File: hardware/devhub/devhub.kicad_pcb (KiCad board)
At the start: 4 copper layers, 100 x 100 mm, 170 parts, among them J1 USB-C PWR IN, J101 USB-C, J2 USB-C UPSTREAM, J201 USB-C, J301 USB-C, J4 SWD, J401 USB-C, J5 Banana COM 1, J6 Banana NC 1, J9 UART debug, K1 G5Q-1 DC5, SW1 Push button switch, generic, 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, SW101 Push button switch, generic, 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, SW201 Push button switch, generic, 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, SW301 Push button switch, generic, 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, SW401 Push button switch, generic, 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, U1 AP7361C-33ER, U101 PI3USB4002A, U12 MCP120T-300I/TT, U13 TPS259470ARPWR, U2 USB2517I-JZX, U201 PI3USB4002A, U3 STM32G0B1CEU6, U301 PI3USB4002A, U4 UCS2114-1-V/LX, U401 PI3USB4002A, U5 UCS2114-1-V/LX, U9 ULN2003V12, Y1 24MHz 12pF

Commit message: U1 thermal vias, wider input zones, GND links at USB-C pins
- U1_HEATSINK: zone reshaped to about 2.6 cm2, 11 vias 0.6/0.3 around
  the tab to the +3V3 plane on In1.Cu instead of 4 vias at the zone edges
- VBUS_IN zone on B.Cu enlarged towards U13, +5V zone corner adjusted
- Port connectors: GND pins tied to the nearby shield pads with 0.6 mm tracks
- C5/C6/C7: GND pads joined with 0.6 mm tracks
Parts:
- C81, R81: moved to F.Cu
- moved TP12 17.8 mm to (143.0, 138.5)
- moved TP14 17.8 mm to (113.0, 138.5)
- moved TP4 11.8 mm to (117.9, 90.6)
- moved TP13 9.77 mm to (128.0, 138.5)
- moved TP11 9.77 mm to (158.0, 138.5)
- moved C81 7.78 mm to (81.8, 122.0)
- moved R81 7.78 mm to (77.0, 122.0)
- moved H1 3.04 mm to (76.7, 103.3)
- moved TP9 2.26 mm to (96.8, 75.5)
- moved J9 2.00 mm to (126.3, 51.5)
- moved TP6 0.10 mm to (95.7, 85.8)
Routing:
- net GND: track 239.3 -> 252.4 mm
- net /Relè ausiliario/BAN1_COM: track 28.8 -> 24.1 mm
- net /Relè ausiliario/K1_NC: track 22.5 -> 17.8 mm
- net VBUS_P2: track 26.6 -> 29.9 mm
- net VBUS_P4: track 26.6 -> 29.9 mm
- net VBUS_P1: track 34.9 -> 32.5 mm
- net VBUS_P3: track 34.9 -> 32.5 mm
- net /MCU STM32G0B1/UART_RX: track 48.4 -> 50.4 mm
- net /MCU STM32G0B1/UART_TX: track 45.1 -> 47.1 mm
- net /Relè ausiliario/BAN1_2: track 29.7 -> 31.7 mm
- net /Relè ausiliario/K1_NO: track 17.5 -> 18.7 mm
- net I2C1_SCL: track 76.9 -> 77.9 mm
- net EFUSE_FLT_N: track 40.7 -> 40.0 mm
- net RLY1: track 105.4 -> 106.0 mm
- net /Alimentazione/VBUS_IN: vias 0 -> 6
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- added copper zone on F.Cu, net +5V
- added copper zone on F.Cu, net /Alimentazione/VBUS_IN
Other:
- board text added: "${TITLE} REV ${REVISION} ${ISSUE_DATE}"

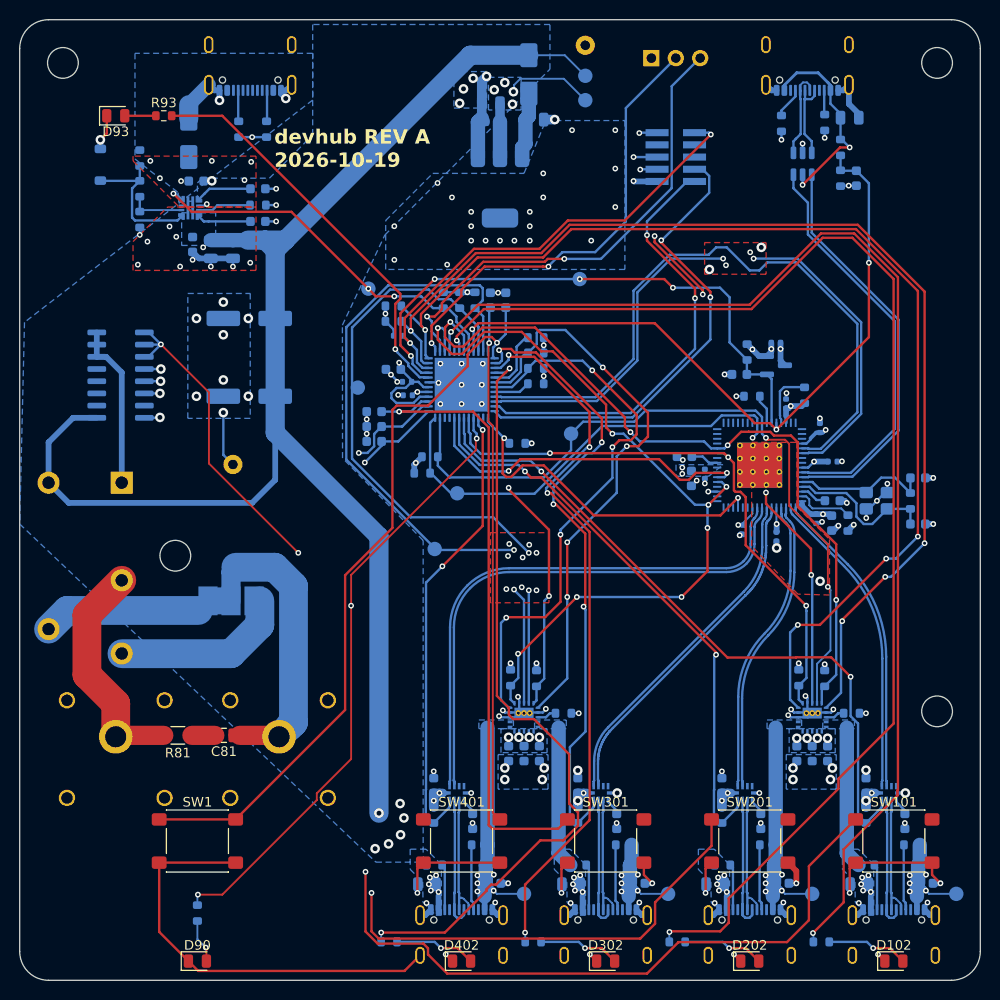
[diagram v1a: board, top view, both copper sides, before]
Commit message: PCB release check: USB_MCU jump on In1.Cu, parity fixes, docs aligned (D94, D95)
PCB: move the USB_MCU_DP crossover jump from In2.Cu to In1.Cu so the GND
plane stays continuous, tune USB_MCU_DN length to pass the skew rule,
remove the leftover "Check LDO pad connection" silkscreen note and update
footprint fields/attributes from the schematic (parity now clean).

Docs: D94 (slow signals and Full-Speed jump on In1.Cu), D95 (H1 hole
position), D52 and D84 marked as superseded on those points; layer table,
port 6 paragraph and manual checks in regole-pcb.md; PCB status, D93 LED
and H1 position in README.md and hardware/README.md.
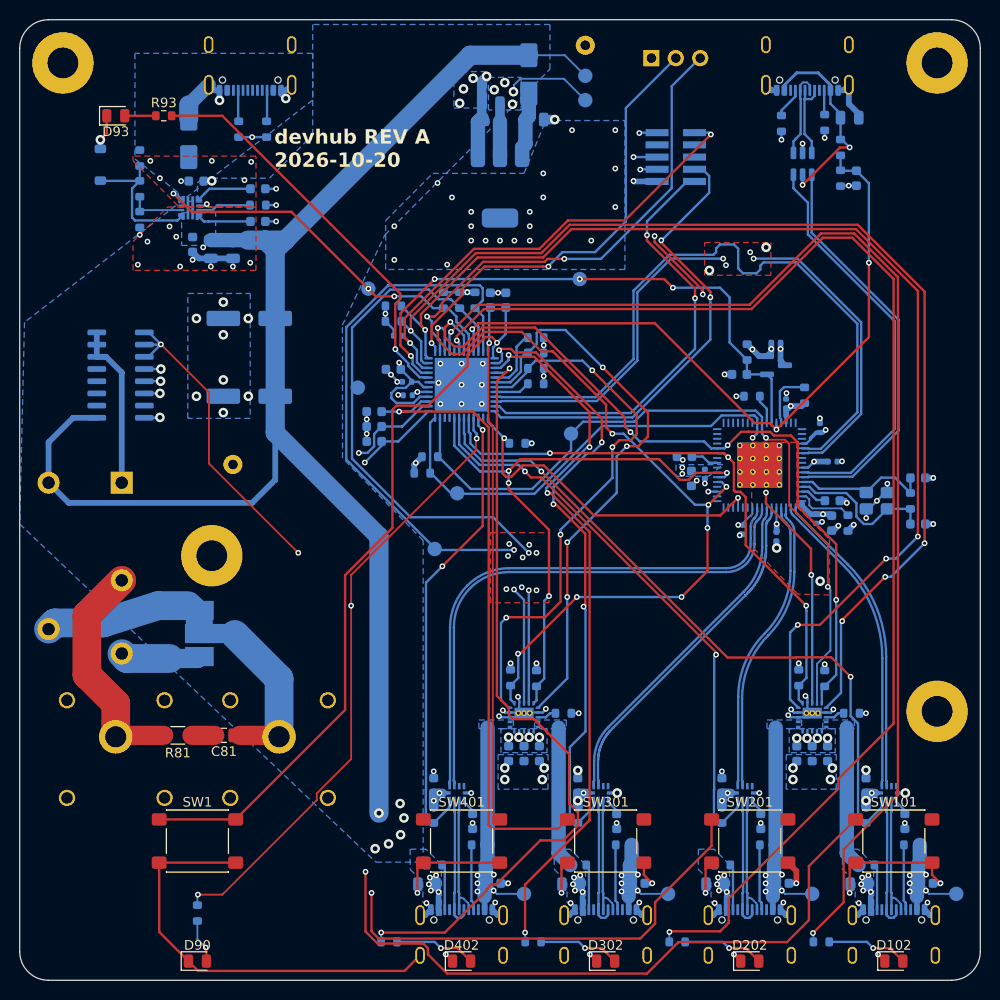
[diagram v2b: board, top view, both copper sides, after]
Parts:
- H1, H2, H3, H4: footprint MountingHole:MountingHole_3.2mm_M3 -> MountingHole:MountingHole_3.2mm_M3_Pad
- moved JP2 4.74 mm to (79.2, 111.4), turned to -90 degrees
- moved H1 3.80 mm to (80.5, 103.3)
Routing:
- net /Relè ausiliario/BAN1_2: track 31.7 -> 21.1 mm
- net /Relè ausiliario/K1_NO: track 18.7 -> 8.37 mm
- net GND: track 252.4 -> 246.6 mm
- net USB_MCU_DN: track 69.0 -> 71.1 mm
- net /Relè ausiliario/K1_NC: track 17.8 -> 16.4 mm
